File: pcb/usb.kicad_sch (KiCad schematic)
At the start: 47 parts, among them J1 Conn_02x03_Counter_Clockwise, J2 USB_B, U6 74LVC1G04, U7 SN74AVC4T245PW, U8 FT2232HQ, U9 93LCxxBxxOT, Y1 12MHz

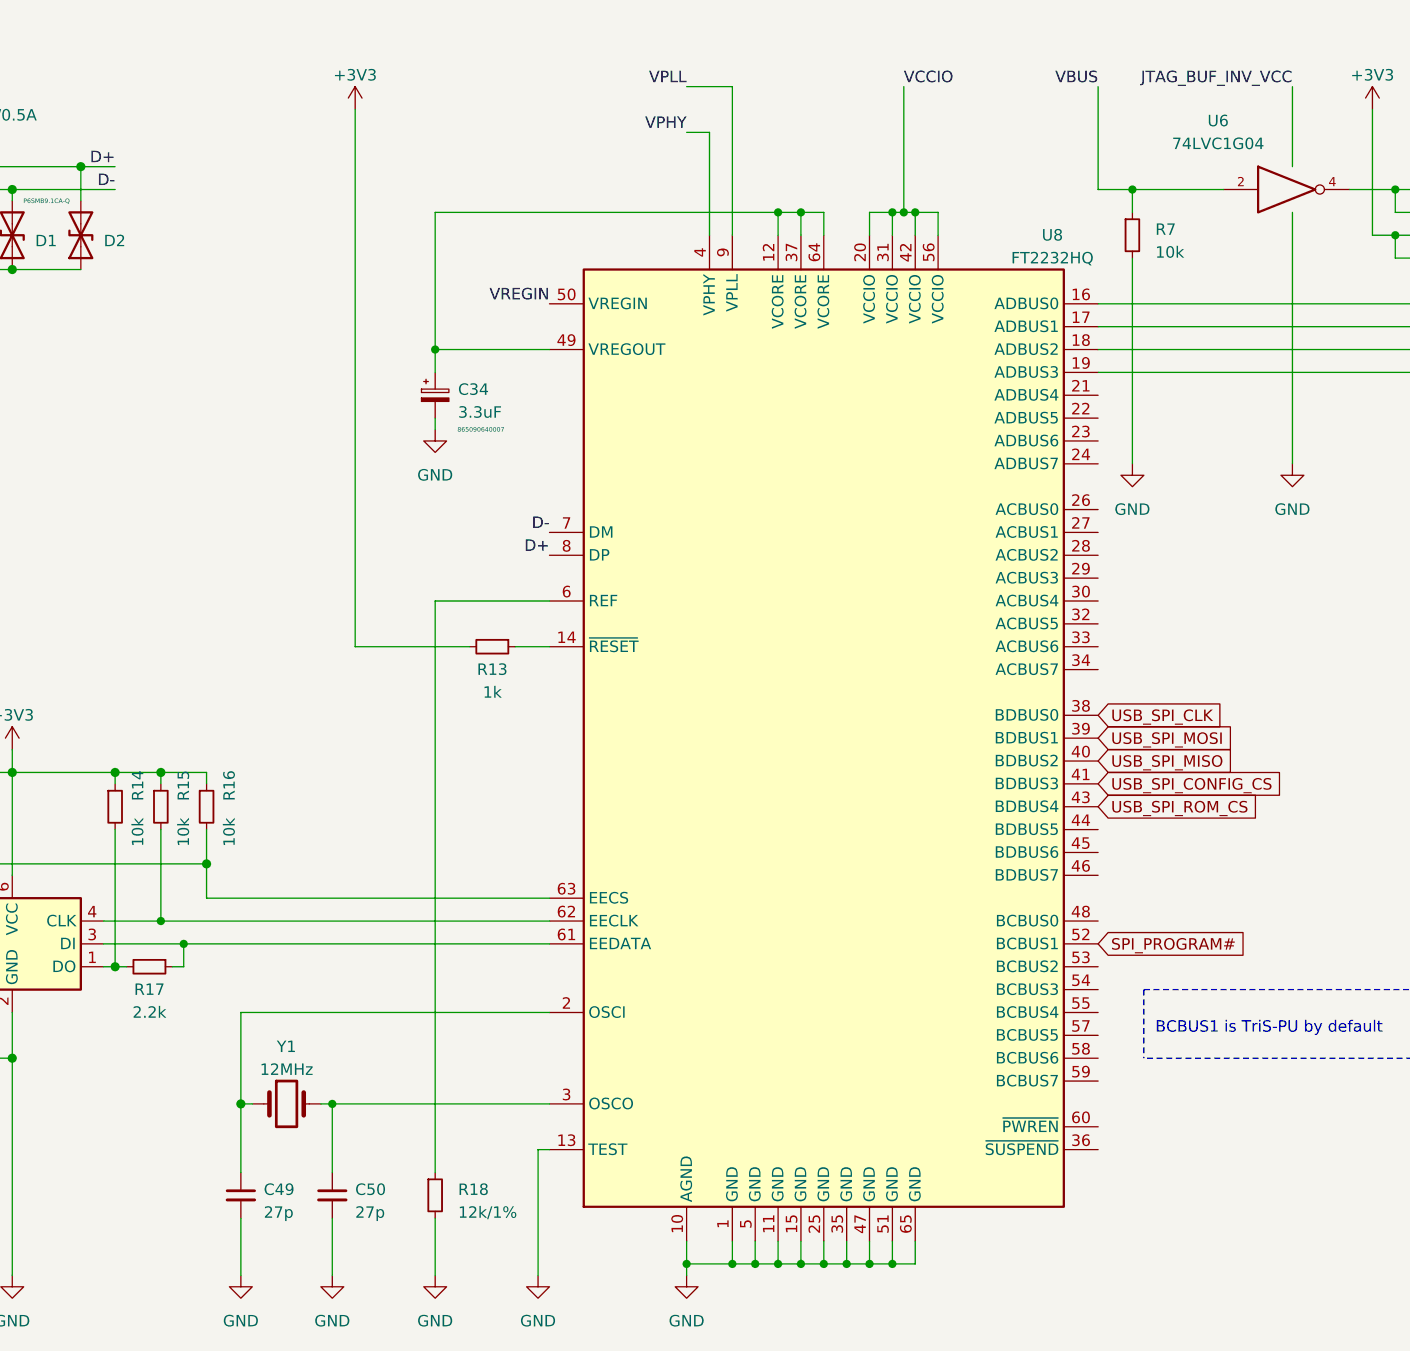
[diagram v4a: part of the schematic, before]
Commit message: add tps541620 footprint
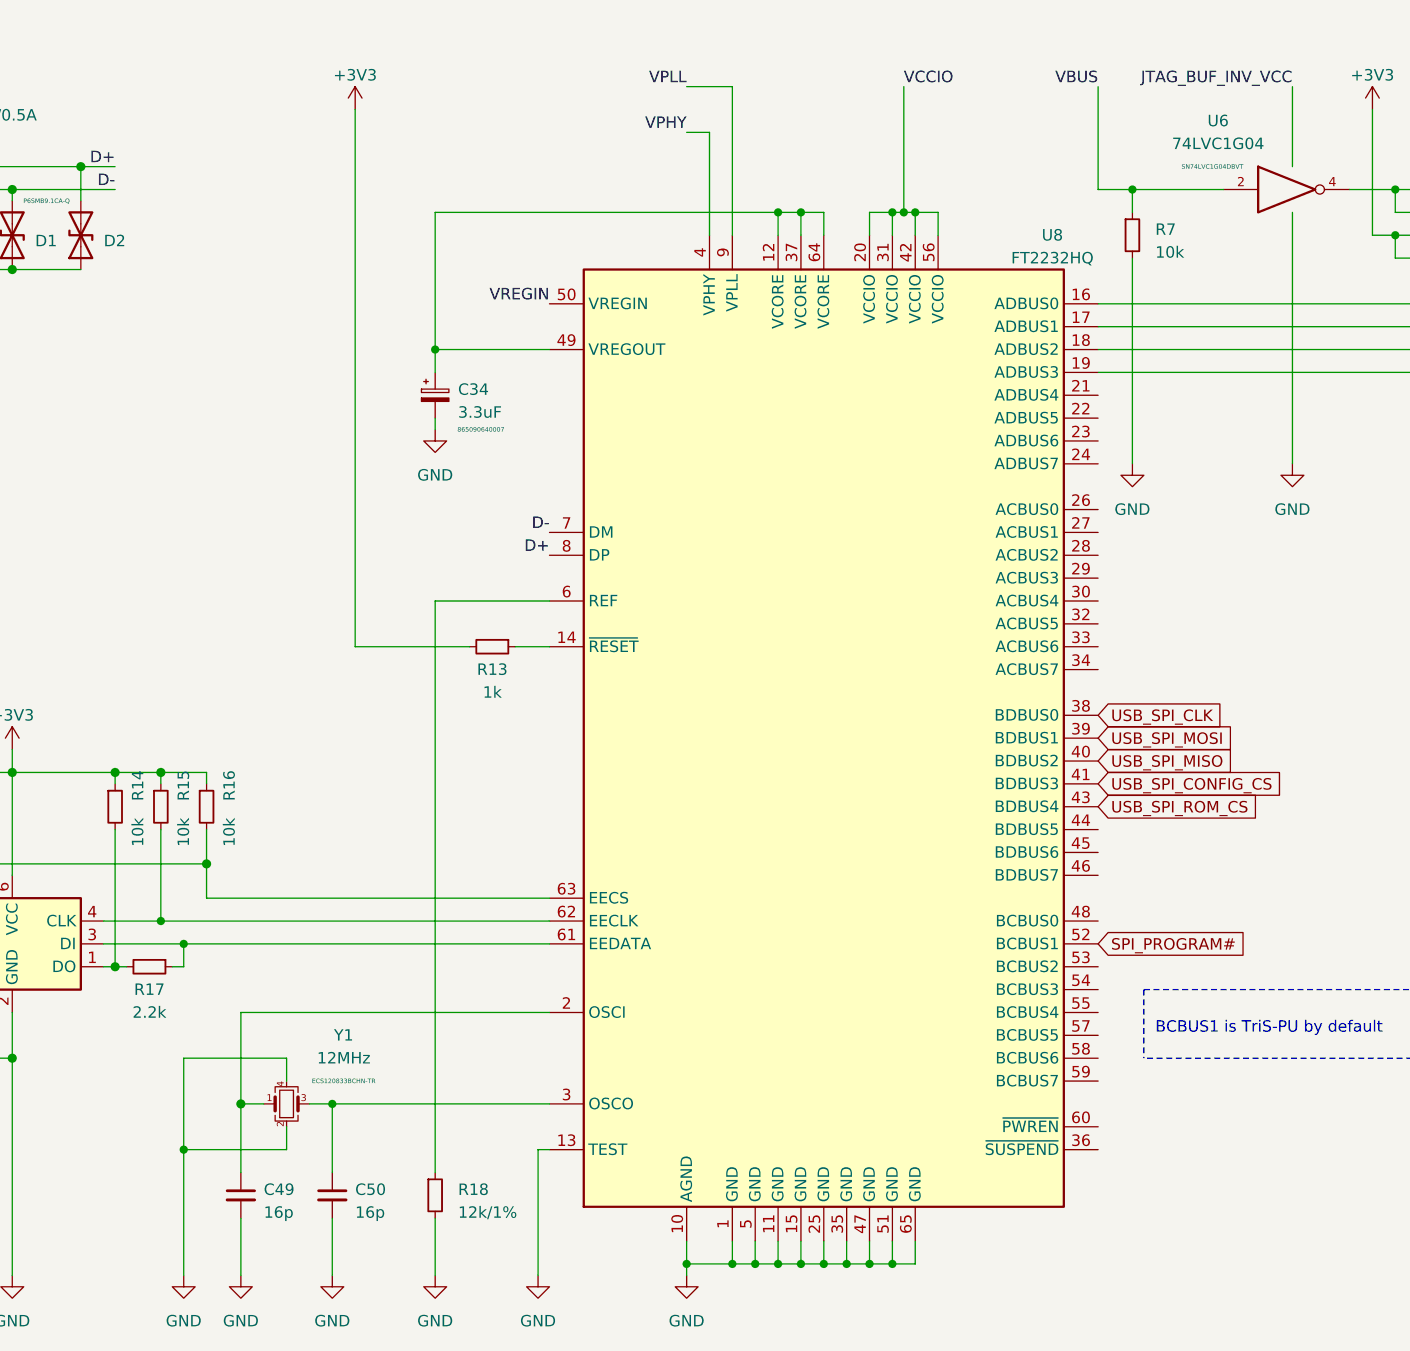
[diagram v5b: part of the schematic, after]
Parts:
- C49, C50: value 27p -> 16p
- J2: footprint (none) -> Connector_USB:BEL_SS-52300-001
- R10, R11, R12, R13, R14, R15, R16, R17, R18, R7, R8, R9: footprint (none) -> Resistor_SMD:R_0402_1005Metric
- U6: footprint (none) -> Package_TO_SOT_SMD:SOT-23-5; Ref (none) -> SN74LVC1G04DBVT
- Y1: footprint (none) -> Crystal:Crystal_SMD_EuroQuartz_MT-4Pin_3.2x2.5mm; symbol Device:Crystal -> Device:Crystal_GND24_Small; Ref (none) -> ECS120833BCHN-TR
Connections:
- net GND: now also Y1.2, Y1.4
- net at C50.1, U8.3 (OSCO): now also Y1.3; no longer Y1.2
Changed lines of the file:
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@@
   (junction (at 138.43 130.81) (diameter 0.9144) (color 0 0 0 0))
   (junction (at 140.97 133.35) (diameter 0.9144) (color 0 0 0 0))
+  (junction (at 140.97 156.21) (diameter 0.9144) (color 0 0 0 0))
   (junction (at 143.51 124.46) (diameter 1.016) (color 0 0 0 0))
   (junction (at 147.32 151.13) (diameter 1.016) (color 0 0 0 0))
@@
     (stroke (width 0) (type solid) (color 0 0 0 0))
   )
+  (wire (pts (xy 140.97 146.05) (xy 152.4 146.05))
+    (stroke (width 0) (type solid) (color 0 0 0 0))
+  )
+  (wire (pts (xy 140.97 156.21) (xy 140.97 146.05))
+    (stroke (width 0) (type solid) (color 0 0 0 0))
+  )
+  (wire (pts (xy 140.97 156.21) (xy 152.4 156.21))
+    (stroke (width 0) (type solid) (color 0 0 0 0))
+  )
+  (wire (pts (xy 140.97 170.18) (xy 140.97 156.21))
+    (stroke (width 0) (type solid) (color 0 0 0 0))
+  )
   (wire (pts (xy 143.51 114.3) (xy 143.51 115.57))
     (stroke (width 0) (type solid) (color 0 0 0 0))
@@
     (stroke (width 0) (type solid) (color 0 0 0 0))
   )
-  (wire (pts (xy 147.32 151.13) (xy 148.59 151.13))
+  (wire (pts (xy 147.32 151.13) (xy 149.86 151.13))
     (stroke (width 0) (type solid) (color 0 0 0 0))
   )
@@
     (stroke (width 0) (type solid) (color 0 0 0 0))
   )
-  (wire (pts (xy 156.21 151.13) (xy 157.48 151.13))
+  (wire (pts (xy 152.4 146.05) (xy 152.4 148.59))
+    (stroke (width 0) (type solid) (color 0 0 0 0))
+  )
+  (wire (pts (xy 152.4 153.67) (xy 152.4 156.21))
+    (stroke (width 0) (type solid) (color 0 0 0 0))
+  )
+  (wire (pts (xy 154.94 151.13) (xy 157.48 151.13))
     (stroke (width 0) (type solid) (color 0 0 0 0))
   )
@@
     (pin "1")
   )
+  (symbol (lib_id "power:GND") (at 140.97 170.18 0) (unit 1)
+    (in_bom yes) (on_board yes)
+    (property "Reference" "#PWR0107" (id 0) (at 140.97 176.53 0)
+      (effects (font (size 1.27 1.27)) hide)
+    )
+    (property "Value" "GND" (id 1) (at 140.97 175.26 0))
+    (property "Footprint" "" (id 2) (at 140.97 170.18 0)
+      (effects (font (size 1.27 1.27)) hide)
+    )
+    (property "Datasheet" "" (id 3) (at 140.97 170.18 0)
+      (effects (font (size 1.27 1.27)) hide)
+    )
+    (pin "1")
+  )
   (symbol (lib_id "power:GND") (at 147.32 170.18 0) (unit 1)
     (in_bom yes) (on_board yes)
@@
       (effects (font (size 1.27 1.27)) (justify left))
     )
-    (property "Footprint" "" (id 2) (at 133.35 118.11 0)
+    (property "Footprint" "Resistor_SMD:R_0402_1005Metric" (id 2) (at 133.35 118.11 0)
       (effects (font (size 1.27 1.27)) hide)
     )
@@
     (property "Reference" "R17" (id 0) (at 137.16 138.43 90))
     (property "Value" "2.2k" (id 1) (at 137.16 140.97 90))
-    (property "Footprint" "" (id 2) (at 137.16 135.89 0)
+    (property "Footprint" "Resistor_SMD:R_0402_1005Metric" (id 2) (at 137.16 135.89 0)
       (effects (font (size 1.27 1.27)) hide)
     )
@@
       (effects (font (size 1.27 1.27)) (justify left))
     )
-    (property "Footprint" "" (id 2) (at 138.43 118.11 0)
+    (property "Footprint" "Resistor_SMD:R_0402_1005Metric" (id 2) (at 138.43 118.11 0)
       (effects (font (size 1.27 1.27)) hide)
     )
@@
       (effects (font (size 1.27 1.27)) (justify left))
     )
-    (property "Footprint" "" (id 2) (at 143.51 118.11 0)
+    (property "Footprint" "Resistor_SMD:R_0402_1005Metric" (id 2) (at 143.51 118.11 0)
       (effects (font (size 1.27 1.27)) hide)
     )
@@
       (effects (font (size 1.27 1.27)) (justify left))
     )
-    (property "Footprint" "" (id 2) (at 168.91 161.29 0)
+    (property "Footprint" "Resistor_SMD:R_0402_1005Metric" (id 2) (at 168.91 161.29 0)
       (effects (font (size 1.27 1.27)) hide)
     )
@@
     (property "Reference" "R13" (id 0) (at 175.26 102.87 90))
     (property "Value" "1k" (id 1) (at 175.26 105.41 90))
-    (property "Footprint" "" (id 2) (at 175.26 100.33 0)
+    (property "Footprint" "Resistor_SMD:R_0402_1005Metric" (id 2) (at 175.26 100.33 0)
       (effects (font (size 1.27 1.27)) hide)
     )
@@
       (effects (font (size 1.27 1.27)) (justify left))
     )
-    (property "Footprint" "" (id 2) (at 246.38 54.61 0)
+    (property "Footprint" "Resistor_SMD:R_0402_1005Metric" (id 2) (at 246.38 54.61 0)
       (effects (font (size 1.27 1.27)) hide)
     )
@@
       (effects (font (size 1.27 1.27)) (justify left))
     )
-    (property "Footprint" "" (id 2) (at 312.42 55.88 0)
+    (property "Footprint" "Resistor_SMD:R_0402_1005Metric" (id 2) (at 312.42 55.88 0)
       (effects (font (size 1.27 1.27)) hide)
     )
@@
       (effects (font (size 1.27 1.27)) (justify left))
     )
-    (property "Footprint" "" (id 2) (at 317.5 55.88 0)
+    (property "Footprint" "Resistor_SMD:R_0402_1005Metric" (id 2) (at 317.5 55.88 0)
       (effects (font (size 1.27 1.27)) hide)
     )
@@
       (effects (font (size 1.27 1.27)) (justify left))
     )
-    (property "Footprint" "" (id 2) (at 322.58 55.88 0)
+    (property "Footprint" "Resistor_SMD:R_0402_1005Metric" (id 2) (at 322.58 55.88 0)
       (effects (font (size 1.27 1.27)) hide)
     )
@@
       (effects (font (size 1.27 1.27)) (justify left))
     )
-    (property "Footprint" "" (id 2) (at 328.93 67.31 0)
+    (property "Footprint" "Resistor_SMD:R_0402_1005Metric" (id 2) (at 328.93 67.31 0)
       (effects (font (size 1.27 1.27)) hide)
     )
@@
       (effects (font (size 1.27 1.27)) (justify left))
     )
-    (property "Footprint" "" (id 2) (at 344.17 67.31 0)
+    (property "Footprint" "Resistor_SMD:R_0402_1005Metric" (id 2) (at 344.17 67.31 0)
       (effects (font (size 1.27 1.27)) hide)
     )
@@
       (effects (font (size 1.27 1.27)) (justify left))
     )
-    (property "Value" "27p" (id 1) (at 149.86 163.1949 0)
+    (property "Value" "16p" (id 1) (at 149.86 163.1949 0)
       (effects (font (size 1.27 1.27)) (justify left))
     )
@@
       (effects (font (size 1.27 1.27)) (justify left))
     )
-    (property "Value" "27p" (id 1) (at 160.02 163.1949 0)
+    (property "Value" "16p" (id 1) (at 160.02 163.1949 0)
       (effects (font (size 1.27 1.27)) (justify left))
     )
@@
     (pin "2")
   )
-  (symbol (lib_id "Device:Crystal") (at 152.4 151.13 0) (unit 1)
-    (in_bom yes) (on_board yes) (fields_autoplaced)
-    (property "Reference" "Y1" (id 0) (at 152.4 144.78 0))
-    (property "Value" "12MHz" (id 1) (at 152.4 147.32 0))
-    (property "Footprint" "" (id 2) (at 152.4 151.13 0)
+  (symbol (lib_id "Device:Crystal_GND24_Small") (at 152.4 151.13 0) (unit 1)
+    (in_bom yes) (on_board yes)
+    (property "Reference" "Y1" (id 0) (at 158.75 143.51 0))
+    (property "Value" "12MHz" (id 1) (at 158.75 146.05 0))
+    (property "Footprint" "Crystal:Crystal_SMD_EuroQuartz_MT-4Pin_3.2x2.5mm" (id 2) (at 152.4 151.13 0)
       (effects (font (size 1.27 1.27)) hide)
     )
@@
       (effects (font (size 1.27 1.27)) hide)
     )
-    (pin "1")
-    (pin "2")
+    (property "Ref" "ECS120833BCHN-TR" (id 4) (at 158.75 148.59 0)
+      (effects (font (size 0.5 0.5)))
+    )
+    (pin "1")
+    (pin "2")
+    (pin "3")
+    (pin "4")
   )
   (symbol (lib_id "74xGxx:74LVC1G04") (at 264.16 49.53 0) (unit 1)
@@
     (property "Reference" "U6" (id 0) (at 255.905 41.91 0))
     (property "Value" "74LVC1G04" (id 1) (at 255.905 44.45 0))
-    (property "Footprint" "" (id 2) (at 264.16 49.53 0)
+    (property "Footprint" "Package_TO_SOT_SMD:SOT-23-5" (id 2) (at 264.16 49.53 0)
       (effects (font (size 1.27 1.27)) hide)
     )
     (property "Datasheet" "http://www.ti.com/lit/sg/scyt129e/scyt129e.pdf" (id 3) (at 264.16 49.53 0)
       (effects (font (size 1.27 1.27)) hide)
+    )
+    (property "Ref" "SN74LVC1G04DBVT" (id 4) (at 255.27 46.99 0)
+      (effects (font (size 0.5 0.5)))
     )
     (pin "2")
@@
     (property "Reference" "J2" (id 0) (at 100.457 33.02 0))
     (property "Value" "USB_B" (id 1) (at 100.457 35.56 0))
-    (property "Footprint" "" (id 2) (at 104.14 48.26 0)
-      (effects (font (size 1.27 1.27)) hide)
-    )
+    (property "Footprint" "Connector_USB:BEL_SS-52300-001" (id 2) (at 104.14 48.26 0)
+      (effects (font (size 1.27 1.27)) hide)
+    )

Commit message: add footprint for the button
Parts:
- J1: footprint (none) -> Connector_PinHeader_2.00mm:PinHeader_1x06_P2.00mm_Vertical
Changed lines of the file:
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@@
       (effects (font (size 1.27 1.27)) hide)
     )
-    (property "Footprint" "" (id 2) (at 351.79 43.18 0)
+    (property "Footprint" "Connector_PinHeader_2.00mm:PinHeader_1x06_P2.00mm_Vertical" (id 2) (at 351.79 43.18 0)
       (effects (font (size 1.27 1.27)) hide)
     )

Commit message: add components to pcb
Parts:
- D1, D2: footprint Package_SO:DO-214AC -> DO-214AC:DO-214AC
- J2: footprint Connector_USB:BEL_SS-52300-001 -> SS-52300-001:BEL_SS-52300-001
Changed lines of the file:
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@@
-(kicad_sch (version 20210126) (generator eeschema)
+(kicad_sch (version 20210406) (generator eeschema)
   (paper "User" 389.992 219.989)
   (title_block
@@
       (effects (font (size 1.27 1.27)) (justify right) hide)
     )
-    (property "Footprint" "Package_SO:DO-214AC" (id 2) (at 121.92 54.61 0)
+    (property "Footprint" "DO-214AC:DO-214AC" (id 2) (at 121.92 54.61 0)
       (effects (font (size 1.27 1.27)) hide)
     )
@@
       (effects (font (size 1.27 1.27)) (justify right) hide)
     )
-    (property "Footprint" "Package_SO:DO-214AC" (id 2) (at 129.54 54.61 0)
+    (property "Footprint" "DO-214AC:DO-214AC" (id 2) (at 129.54 54.61 0)
       (effects (font (size 1.27 1.27)) hide)
     )
@@
     (property "Reference" "J2" (id 0) (at 100.457 33.02 0))
     (property "Value" "USB_B" (id 1) (at 100.457 35.56 0))
-    (property "Footprint" "Connector_USB:BEL_SS-52300-001" (id 2) (at 104.14 48.26 0)
-      (effects (font (size 1.27 1.27)) hide)
-    )
+    (property "Footprint" "SS-52300-001:BEL_SS-52300-001" (id 2) (at 104.14 48.26 0)
+      (effects (font (size 1.27 1.27)) hide)
+    )

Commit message: start placing components
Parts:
- C34: footprint Capacitor_SMD:CP_Elec_4x4.5 -> Capacitor_SMD:C_1210_3225Metric; symbol Device:C_Polarized_Small -> Device:C_Small; Ref 865090640007 -> GRM32ER60J107ME20L
